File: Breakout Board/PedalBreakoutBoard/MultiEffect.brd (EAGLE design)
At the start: 61.9 x 86.3 mm, 69 parts, among them IC1 LD1117V, IC2 MCP6004P, U1 OPA1652AID

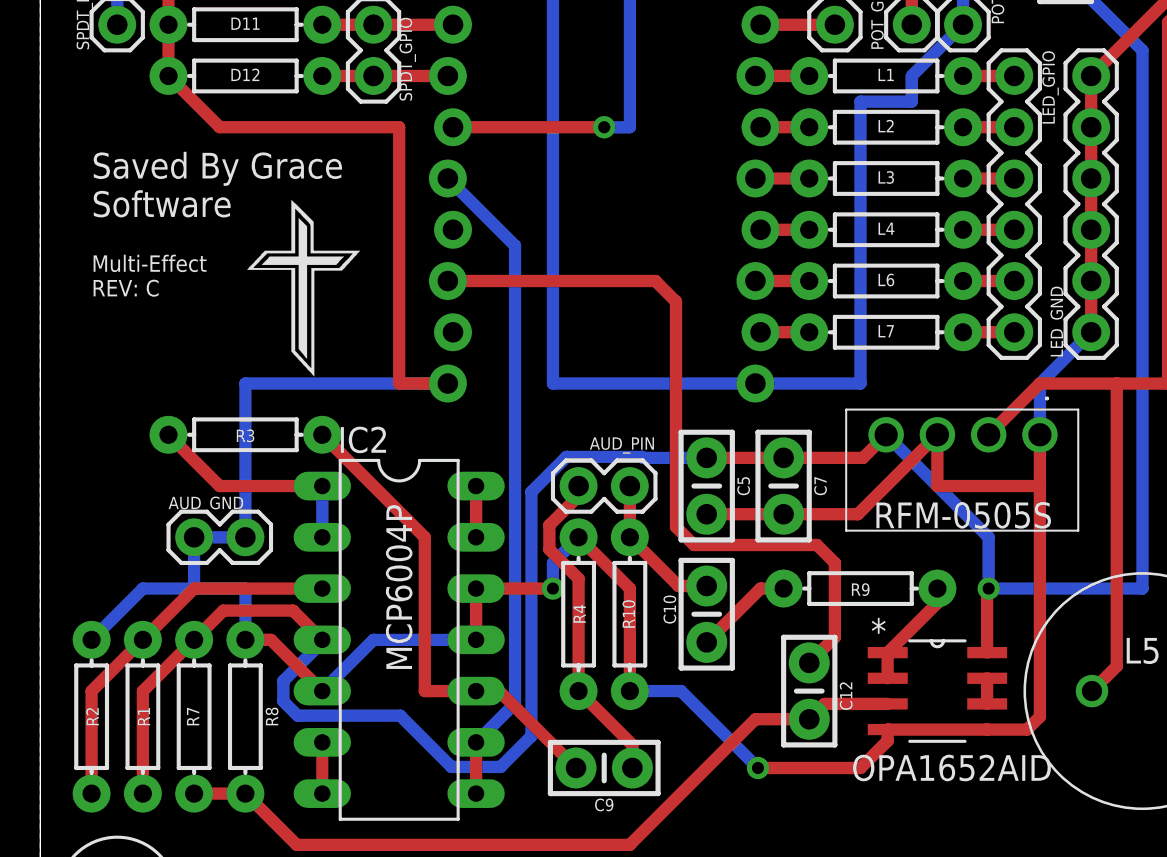
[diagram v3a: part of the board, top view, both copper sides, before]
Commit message: DP-97 - Update multi-effect with new grounding scheme
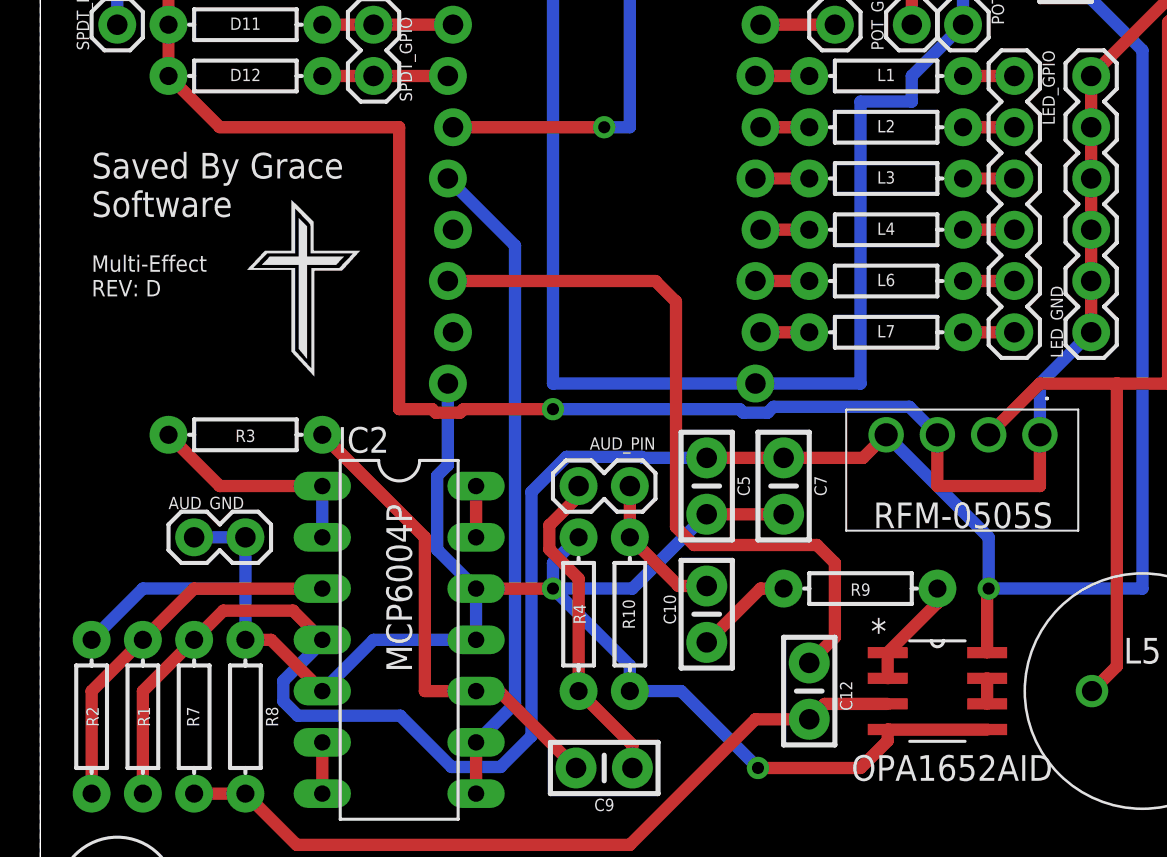
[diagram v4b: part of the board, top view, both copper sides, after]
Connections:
- new net AGND: AUD_GND.1, AUD_GND.2, C5.2, C7.2, IC2.11, IC2.12, IC2.5, R10.P$1, R2.P$1, R4.P$1, R8.P$1, SEED.20, U1.4, U1.5
- net GND: no longer AUD_GND.1, AUD_GND.2, C5.2, C7.2, IC2.11, IC2.12, IC2.5, R10.P$1, R2.P$1, R4.P$1, R8.P$1, SEED.20, U1.4, U1.5
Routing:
- net AGND: track 0.00 -> 90.4 mm, vias 0 -> 2
- net GND: track 315.8 -> 228.9 mm, vias 2 -> 1
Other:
- board text added: "Multi-Effect REV: D"
- board text removed: "Multi-Effect REV: C"
